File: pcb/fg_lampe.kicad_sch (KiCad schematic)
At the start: 13 parts, among them J1 ISP Port, U1 ATmega328P-P, U2 L7805, Y1 16MHz

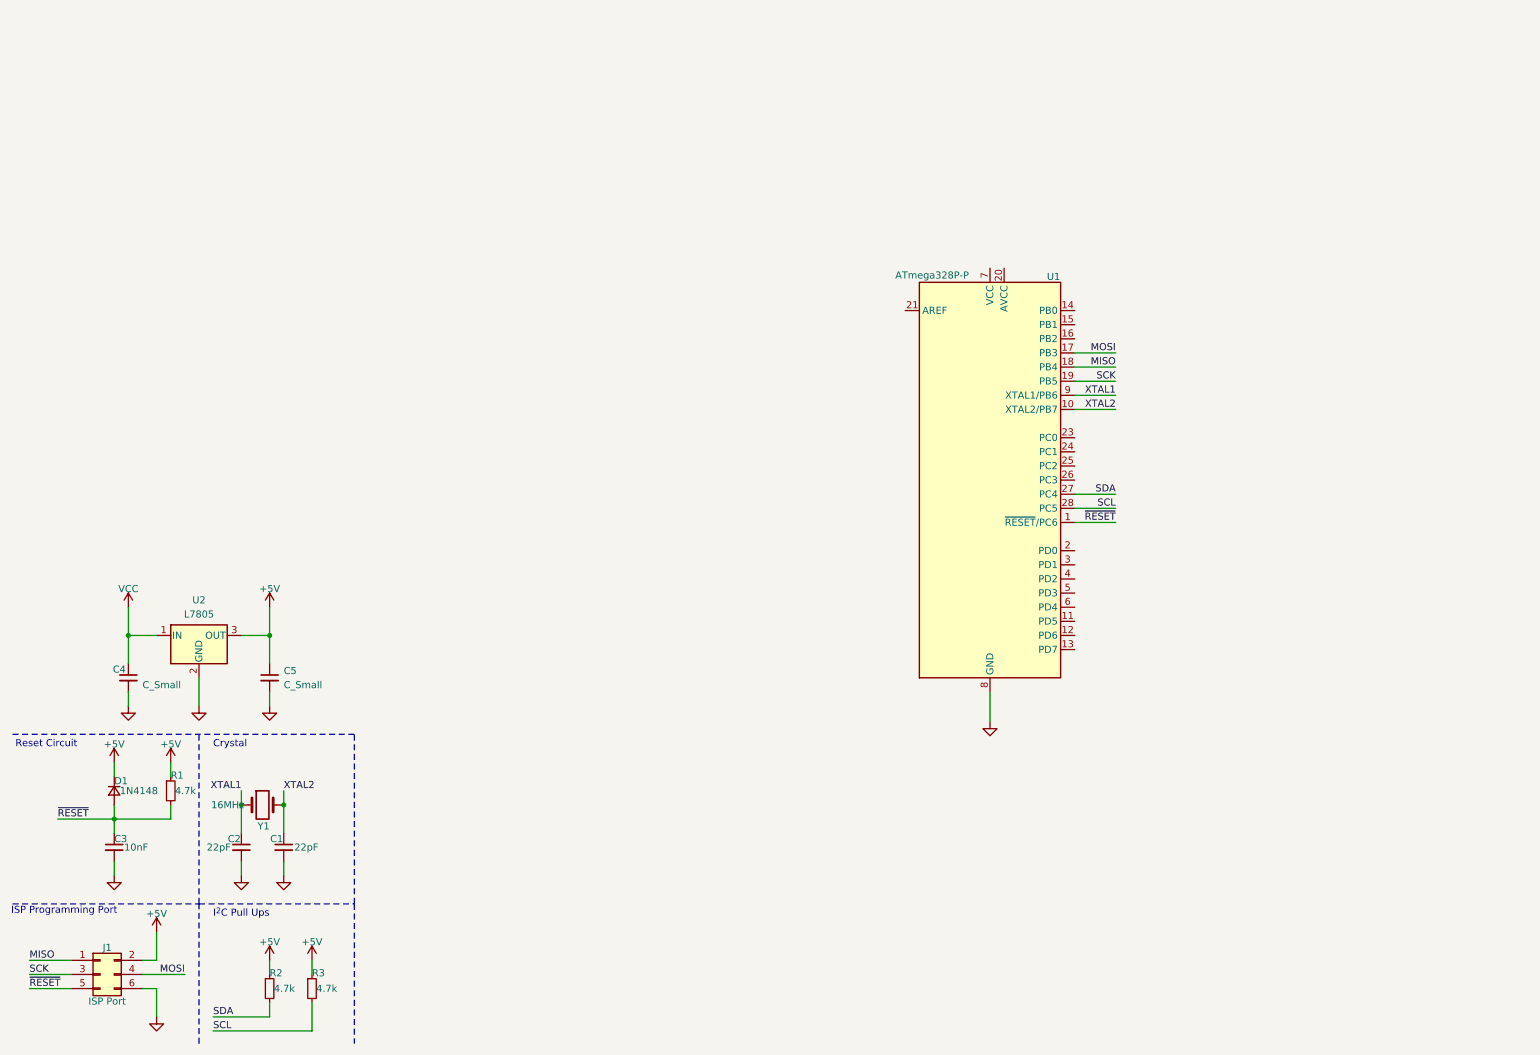
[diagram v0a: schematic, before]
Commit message: negative voltage charge pump added and some minor fixes
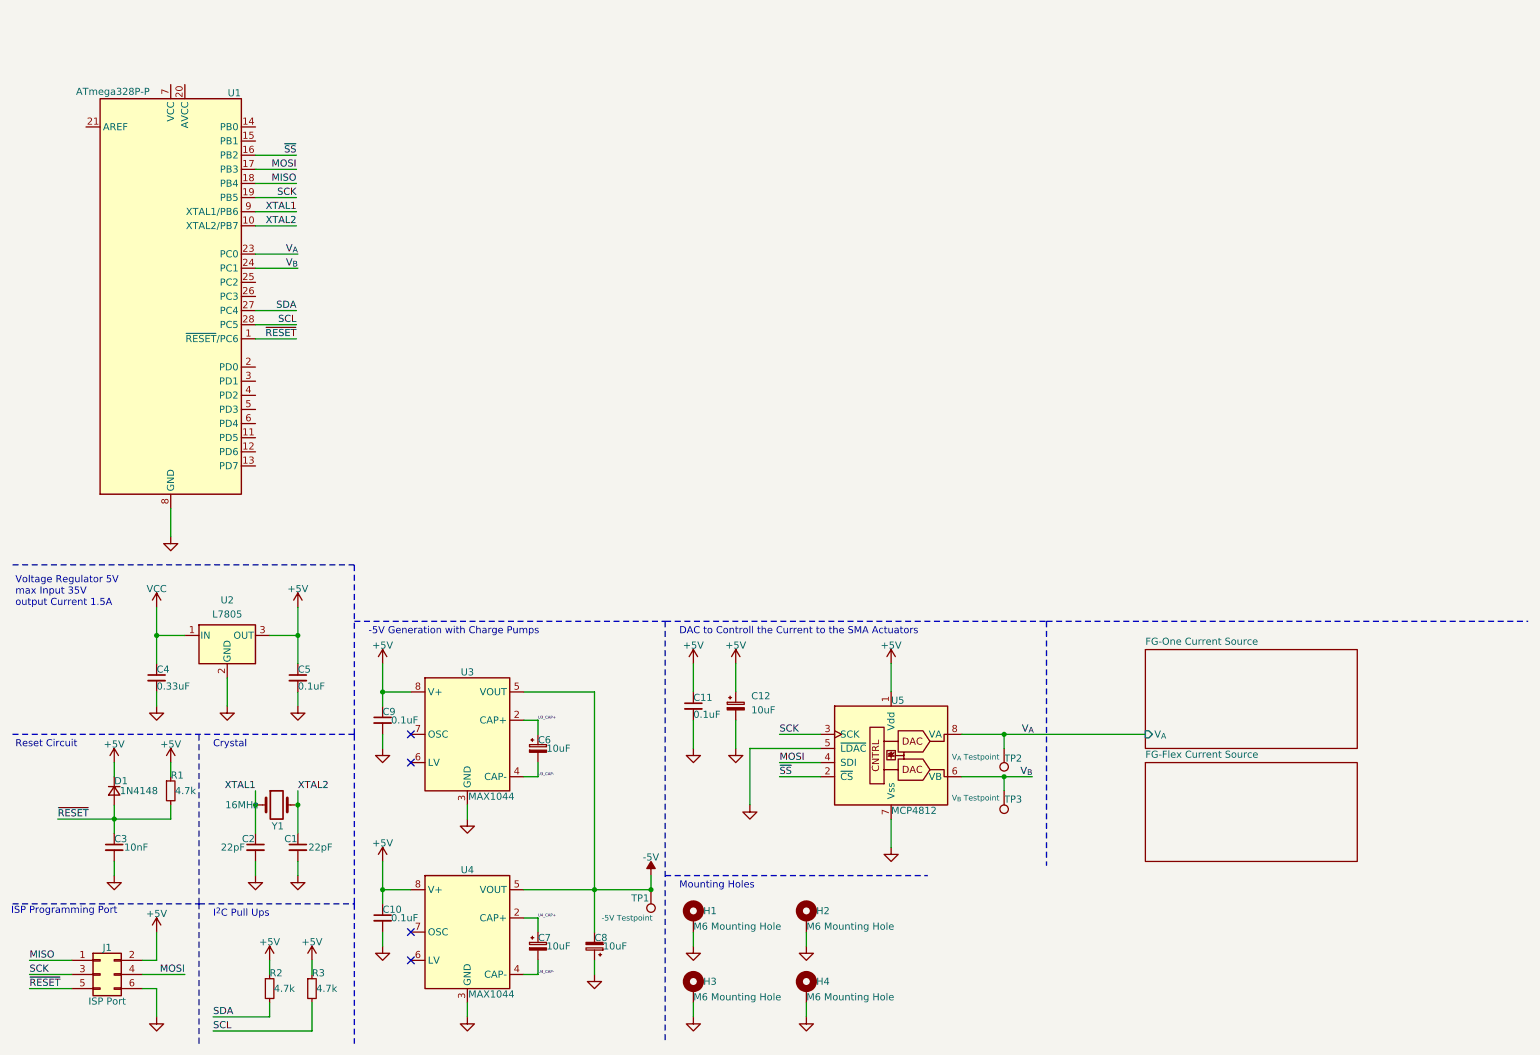
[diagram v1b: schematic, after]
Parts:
- added C10, C11, C9: 0.1uF, Capacitor_THT:C_Disc_D5.1mm_W3.2mm_P5.00mm, symbol Device:C_Small
- added C12: 10uF, Capacitor_THT:CP_Radial_Tantal_D6.0mm_P2.50mm, symbol Device:C_Polarized_Small
- added C6, C7, C8: 10uF, Capacitor_THT:CP_Radial_D5.0mm_P2.00mm, symbol Device:C_Polarized_Small
- added H1, H2, H3, H4: M6 Mounting Hole, MountingHole:MountingHole_6.5mm_Pad_Via, symbol Mechanical:MountingHole_Pad
- added TP1: -5V Testpoint, TestPoint:TestPoint_Pad_D1.0mm, symbol Connector:TestPoint
- added TP2: V_{A} Testpoint, TestPoint:TestPoint_Pad_D1.0mm, symbol Connector:TestPoint
- added TP3: V_{B} Testpoint, TestPoint:TestPoint_Pad_D1.0mm, symbol Connector:TestPoint
- added U3, U4: MAX1044, Package_DIP:DIP-8_W7.62mm, symbol Regulator_SwitchedCapacitor:MAX1044
- added U5: MCP4812, Package_DIP:DIP-8_W7.62mm, symbol Analog_DAC:MCP4812
- C4: value C_Small -> 0.33uF; footprint (none) -> Capacitor_THT:C_Disc_D5.1mm_W3.2mm_P5.00mm; Manufacturer (none) -> KYOCERA AVX; Part Nr.  (none) -> SR215C334KAR
- C5: value C_Small -> 0.1uF; footprint (none) -> Capacitor_THT:C_Disc_D5.1mm_W3.2mm_P5.00mm; Manufacturer (none) -> KYOCERA AVX; Part Nr.  (none) -> SR211C104KARTR1
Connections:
- net +5V: now also C10.1, C11.1, C12.1, C9.1, U3.8 (V+), U4.8 (V+), U5.1 (Vdd)
- net GND: now also C10.2, C11.2, C12.2, C8.1, C9.2, H1.1, H2.1, H3.1, H4.1, U3.3 (GND), U4.3 (GND), U5.5 (~{LDAC}), U5.7 (Vss)
- net MOSI: now also U5.4 (SDI)
- net SCK: now also U5.3 (SCK)
- net ~{SS}: now reaches U1.16 (PB2)
- net ~{SS}: now also U5.2 (~{CS})
- net V_{A}: now reaches U1.23 (PC0)
- net V_{A}: now also TP2.1, U5.8 (VA)
- net V_{B}: now reaches U1.24 (PC1)
- net V_{B}: now also TP3.1, U5.6 (VB)
- new net -5V: C8.2, TP1.1, U3.5 (VOUT), U4.5 (VOUT)
- new net U3_CAP+: C6.1, U3.2 (CAP+)
- new net U3_CAP-: C6.2, U3.4 (CAP-)
- new net U4_CAP+: C7.1, U4.2 (CAP+)
- new net U4_CAP-: C7.2, U4.4 (CAP-)
- no-connect marks 0 -> 4
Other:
- added sheet FG-Flex Current Source (fg-flex_current_source.kicad_sch)
- added sheet FG-One Current Source (fg-one_current_source.kicad_sch)
- note added: "-5V Generation with Charge Pumps"
- note added: "DAC to Controll the Current to the SMA Actuators"
- note added: "Mounting Holes"
- note added: "Voltage Regulator 5V max Input 35V output Current 1.5A"
- title: (none) -> Microcontroller und Peripherie
- moved on the sheet: C1, C2, C4, C5, U1, U2, Y1

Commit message: current sources added
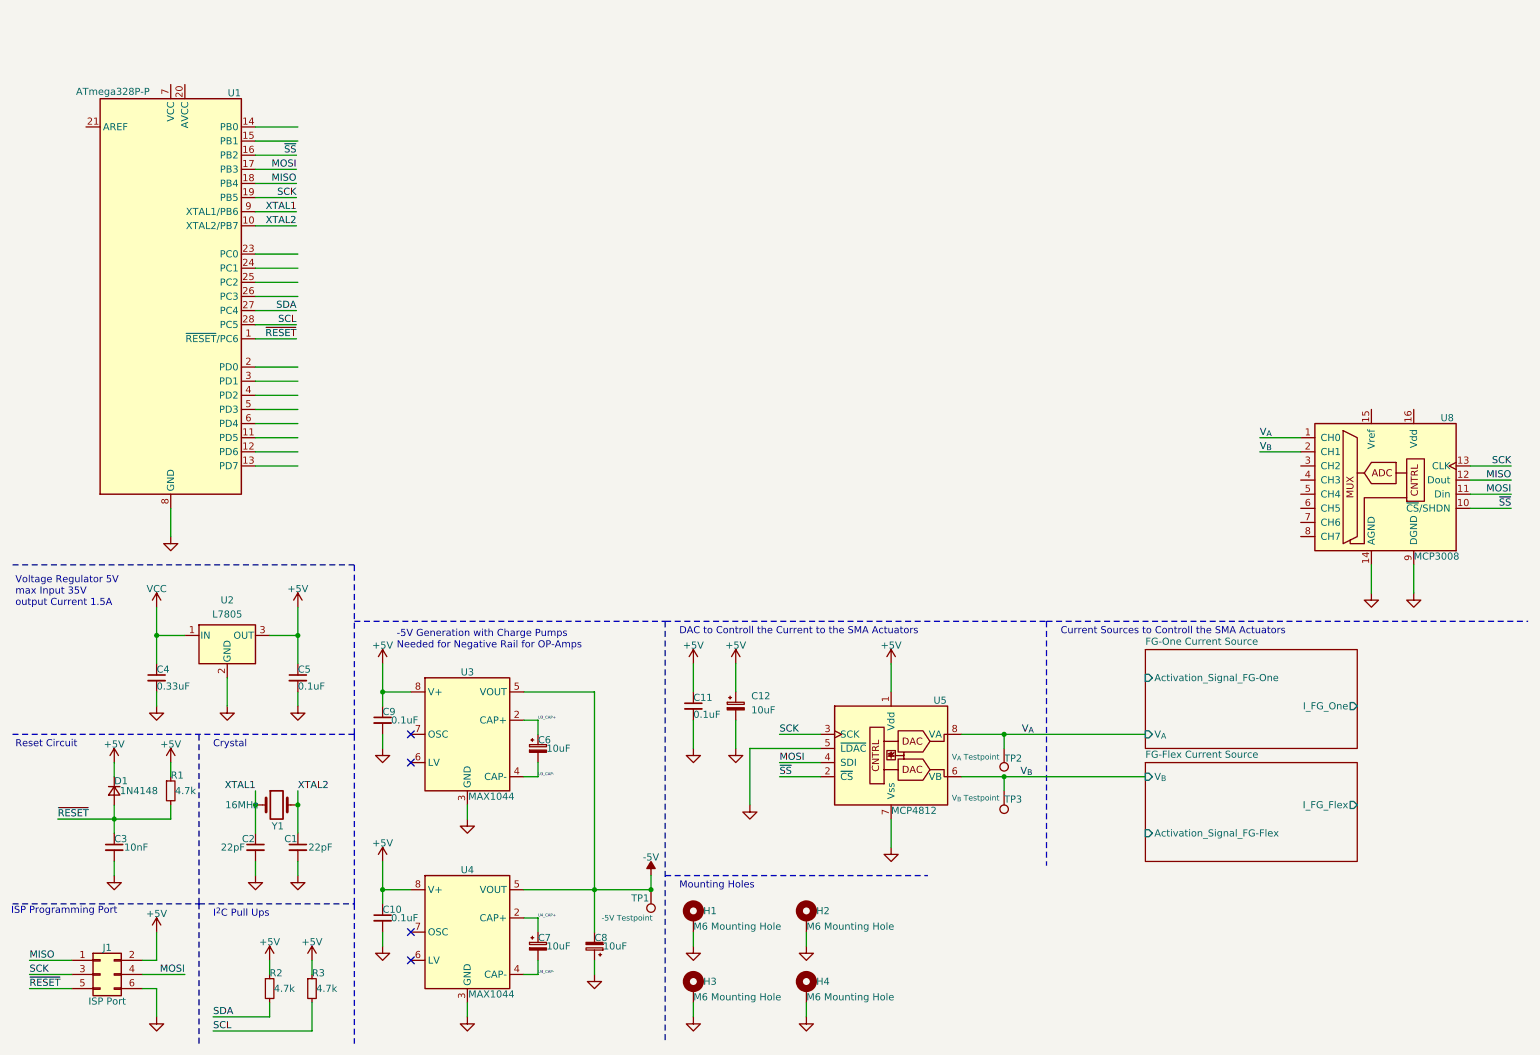
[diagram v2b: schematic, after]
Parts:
- added U8: MCP3008, Package_DIP:DIP-16_W7.62mm_Socket_LongPads, symbol Analog_ADC:MCP3008
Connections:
- net GND: now also U8.14 (AGND), U8.9 (DGND)
- net MISO: now also U8.12 (Dout)
- net MOSI: now also U8.11 (Din)
- net SCK: now also U8.13 (CLK)
- net V_{A}: now also U8.1 (CH0); no longer U1.23 (PC0)
- net V_{B}: now also U8.2 (CH1); no longer U1.24 (PC1)
- net ~{SS}: now also U8.10 (~{CS}/SHDN)
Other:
- sheet FG-Flex Current Source ports: added Activation_Signal_FG-Flex, I_FG_Flex, V_{B}; removed none
- sheet FG-One Current Source ports: added Activation_Signal_FG-One, I_FG_One; removed none
- note added: "-5V Generation with Charge Pumps Needed for Negative Rail for OP-Amps"
- note added: "Current Sources to Controll the SMA Actuators"
- note removed: "-5V Generation with Charge Pumps"

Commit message: mcp3008 finished integrating
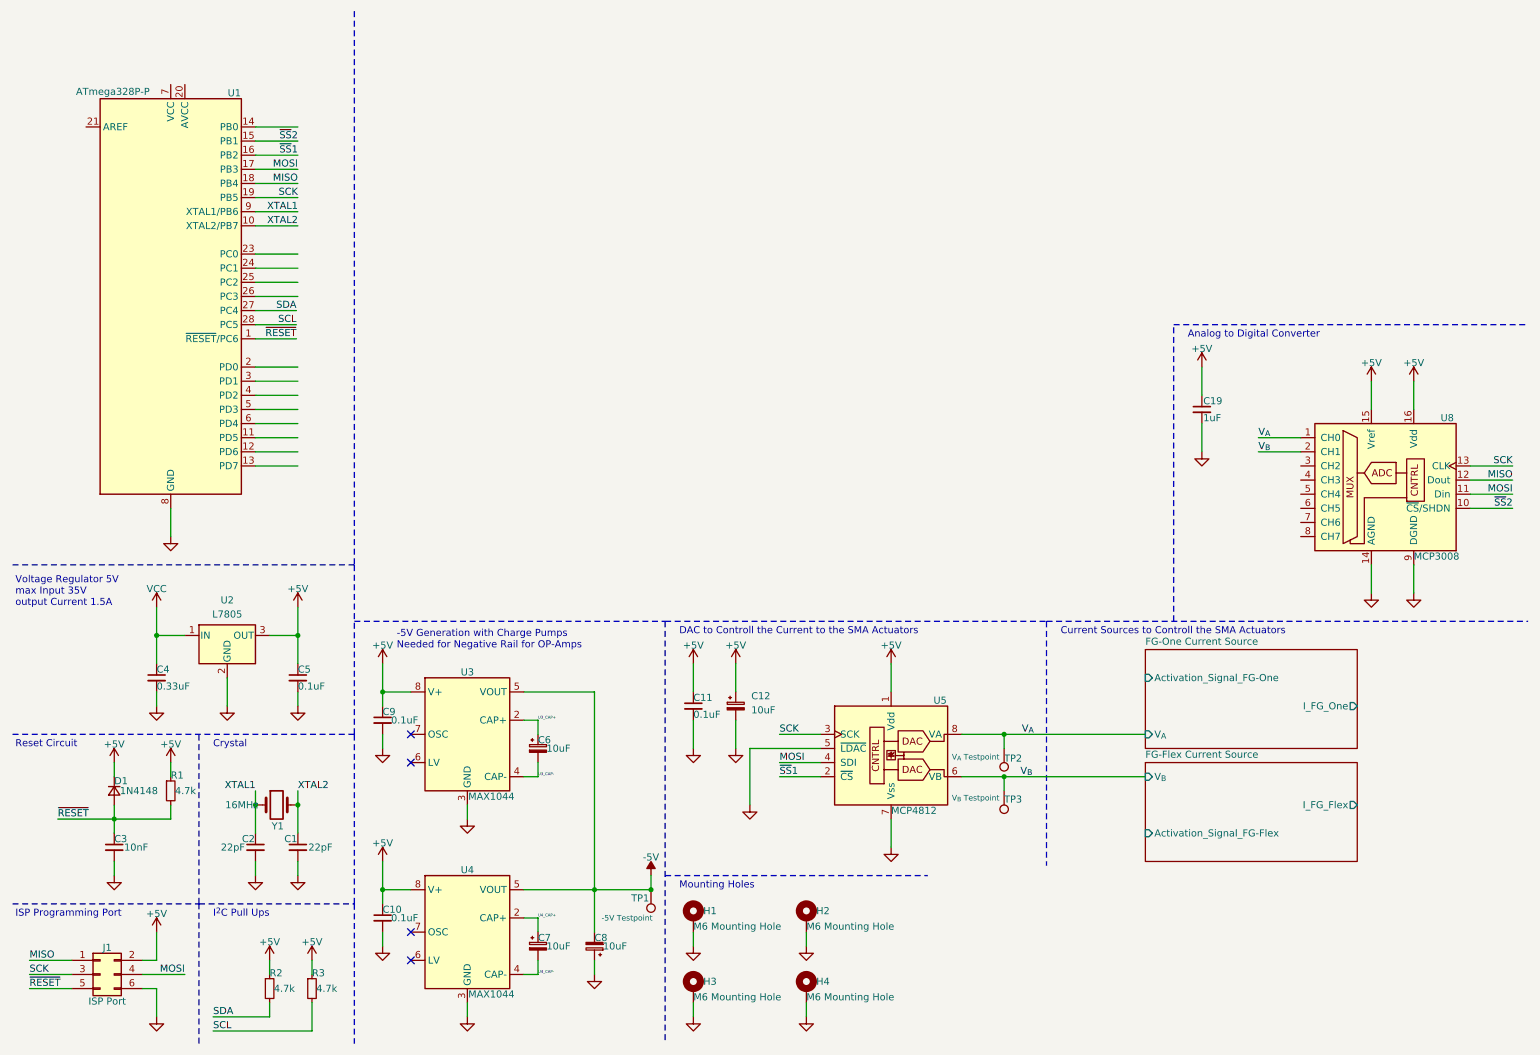
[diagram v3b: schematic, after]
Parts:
- added C19: 1uF, Capacitor_THT:C_Disc_D4.7mm_W2.5mm_P5.00mm, symbol Device:C_Small
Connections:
- net +5V: now also U8.15 (Vref), U8.16 (Vdd), C19.1
- net GND: now also C19.2
- net ~{SS}2: now reaches U1.15 (PB1)
- net ~{SS}2: now also U8.10 (~{CS}/SHDN)
- net ~{SS} renamed ~{SS}1
- net ~{SS}1: no longer U8.10 (~{CS}/SHDN)
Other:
- note added: "Analog to Digital Converter"

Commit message: shunt measurement changed to different opamp
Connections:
- net shunt_fg-one: now reaches U8.3 (CH2)
- net shunt_fg-flex: now reaches U8.4 (CH3)
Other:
- sheet FG-Flex Current Source ports: added shunt_fg-flex; removed none
- sheet FG-One Current Source ports: added shunt_fg-one; removed none
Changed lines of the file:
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@@
+    (stroke (width 0) (type default))
+  )
+  (wire (pts (xy 254 149.86) (xy 269.24 149.86))
     (stroke (width 0) (type default))
   )
@@
     (stroke (width 0) (type default))
   )
-  (wire (pts (xy 236.22 88.9) (xy 243.84 88.9))
+  (wire (pts (xy 228.854 88.9) (xy 243.84 88.9))
+    (stroke (width 0) (type default))
+  )
+  (wire (pts (xy 243.84 96.52) (xy 228.6 96.52))
     (stroke (width 0) (type default))
   )
@@
     (stroke (width 0) (type default))
   )
-  (wire (pts (xy 236.22 91.44) (xy 243.84 91.44))
+  (wire (pts (xy 228.854 91.44) (xy 243.84 91.44))
     (stroke (width 0) (type default))
   )
@@
     (stroke (width 0) (type default))
   )
+  (wire (pts (xy 243.84 93.98) (xy 228.6 93.98))
+    (stroke (width 0) (type default))
+  )
   (wire (pts (xy 48.26 193.04) (xy 58.42 193.04))
     (stroke (width 0) (type default))
@@
   )
   (wire (pts (xy 142.24 139.7) (xy 142.24 144.78))
+    (stroke (width 0) (type default))
+  )
+  (wire (pts (xy 254 142.24) (xy 269.24 142.24))
     (stroke (width 0) (type default))
   )
@@
     (effects (font (size 1.27 1.27)) (justify left bottom))
   )
+  (label "shunt_fg-flex" (at 228.6 96.52 0) (fields_autoplaced)
+    (effects (font (size 1.27 1.27)) (justify left bottom))
+  )
   (label "~{SS}2" (at 63.5 35.56 180) (fields_autoplaced)
     (effects (font (size 1.27 1.27)) (justify right bottom))
@@
     (effects (font (size 1.27 1.27)) (justify right bottom))
   )
+  (label "shunt_fg-one" (at 228.6 93.98 0) (fields_autoplaced)
+    (effects (font (size 1.27 1.27)) (justify left bottom))
+  )
   (label "SCK" (at 281.94 93.98 180) (fields_autoplaced)
     (effects (font (size 1.27 1.27)) (justify right bottom))
@@
     (effects (font (size 1.27 1.27)) (justify right bottom))
   )
-  (label "V_{B}" (at 236.22 91.44 0) (fields_autoplaced)
+  (label "V_{B}" (at 228.854 91.44 0) (fields_autoplaced)
     (effects (font (size 1.27 1.27)) (justify left bottom))
   )
   (label "~{RESET}" (at 15.24 187.96 0) (fields_autoplaced)
     (effects (font (size 1.27 1.27)) (justify left bottom))
+  )
+  (label "shunt_fg-flex" (at 269.24 149.86 180) (fields_autoplaced)
+    (effects (font (size 1.27 1.27)) (justify right bottom))
+  )
+  (label "shunt_fg-one" (at 269.24 142.24 180) (fields_autoplaced)
+    (effects (font (size 1.27 1.27)) (justify right bottom))
   )
   (label "XTAL1" (at 55.88 152.4 180) (fields_autoplaced)
@@
     (effects (font (size 0.5 0.5)) (justify left bottom))
   )
-  (label "V_{A}" (at 236.22 88.9 0) (fields_autoplaced)
+  (label "V_{A}" (at 228.854 88.9 0) (fields_autoplaced)
     (effects (font (size 1.27 1.27)) (justify left bottom))
   )
@@
       (effects (font (size 1.27 1.27)) (justify right))
     )
+    (pin "shunt_fg-flex" output (at 254 149.86 0)
+      (effects (font (size 1.27 1.27)) (justify right))
+    )
     (instances
       (project "fg_lampe"
@@
       (effects (font (size 1.27 1.27)) (justify right))
     )
+    (pin "shunt_fg-one" output (at 254 142.24 0)
+      (effects (font (size 1.27 1.27)) (justify right))
+    )

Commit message: connector added
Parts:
- added J2: I^{2}C Debug, Connector_PinHeader_2.54mm:PinHeader_1x03_P2.54mm_Vertical, symbol Connector:Conn_01x03_Pin
- added J3: RX/TX, Connector_PinHeader_2.54mm:PinHeader_1x04_P2.54mm_Vertical, symbol Connector:Conn_01x04_Pin
- added J4, J5, J6: 1792863, phoenix-contact_connector:TE_1792863, symbol COMBICON PTS Connector:1792863
- U1: footprint Package_DIP:DIP-28_W7.62mm -> Package_DIP:DIP-28_W7.62mm_Socket_LongPads
- U3, U4, U5: footprint Package_DIP:DIP-8_W7.62mm -> Package_DIP:DIP-8_W7.62mm_Socket_LongPads
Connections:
- net +5V: now also J3.4 (Pin_4)
- net GND: now also J2.1 (Pin_1), J3.1 (Pin_1), J4.2, J5.2, J6.2
- net SCL: now also J2.3 (Pin_3)
- net SDA: now also J2.2 (Pin_2)
- net VCC: now also J4.1
- new net I_FG_Flex: J6.1
- new net I_FG_one: J5.1
- new net RX: J3.3 (Pin_3)
- new net TX: J3.2 (Pin_2)
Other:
- note added: "Debug Pins"
- note added: "Power and SMA Connectors"
